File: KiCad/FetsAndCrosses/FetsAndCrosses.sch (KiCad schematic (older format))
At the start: 30 parts, among them J1 9Vdc, U1 L7805

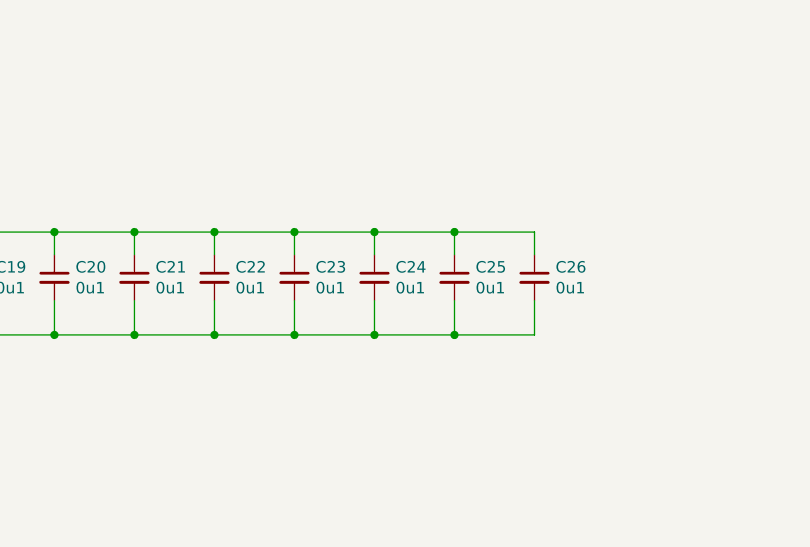
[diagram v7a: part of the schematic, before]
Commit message: Updated Schematic
 - Fixed Mem cell
 - Fixed Draw LED to not light if last move wins game
 - Changed capacitor
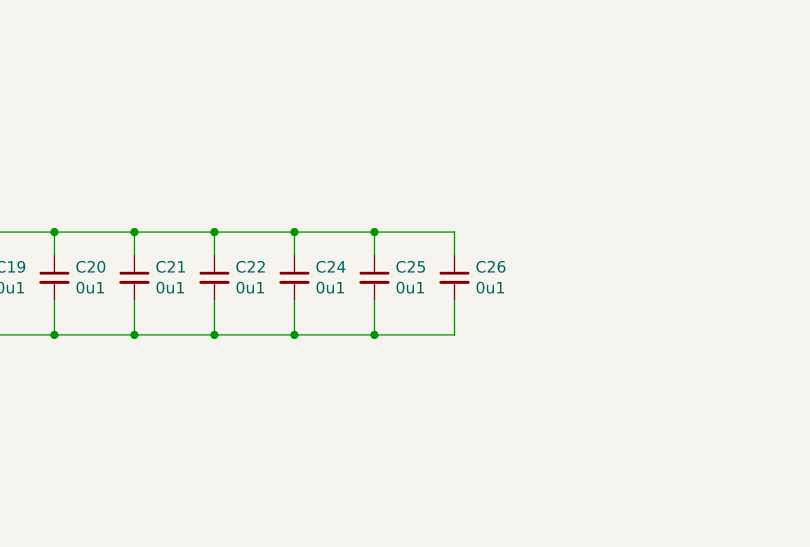
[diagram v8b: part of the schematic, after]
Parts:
- removed C23: 0u1, LogicQ:C_0603_1608Metric_NOLBL, symbol Device:C_Small
- C3: footprint Capacitor_Tantalum_SMD:CP_EIA-6032-15_Kemet-U -> Capacitor_SMD:CP_Elec_6.3x7.7
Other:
- moved on the sheet: C24, C25, C26
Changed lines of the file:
@@
 $Descr A3 16535 11693
 encoding utf-8
-Sheet 1 360
+Sheet 1 362
 Title "Fets and Crosses"
-Date "2020-08-28"
-Rev "v0.1"
+Date "2020-09-15"
+Rev "v0.2"
 Comp "Philipp Schilk"
 Comment1 "Tic-Tac-Toe implementation from discrete-transistor CMOS logic"
@@
 F 0 "C3" H 4141 9996 50  0000 L CNN
 F 1 "10u" H 4141 9905 50  0000 L CNN
-F 2 "Capacitor_Tantalum_SMD:CP_EIA-6032-15_Kemet-U" H 4050 9950 50  0001 C CNN
+F 2 "Capacitor_SMD:CP_Elec_6.3x7.7" H 4050 9950 50  0001 C CNN
 F 3 "~" H 4050 9950 50  0001 C CNN
 	1    4050 9950
@@
 $EndComp
 $Comp
-L Device:C_Small C23
-U 1 1 5F124EFA
+L Device:C_Small C24
+U 1 1 5F124F00
 P 9450 9950
-F 0 "C23" H 9542 9996 50  0000 L CNN
+F 0 "C24" H 9542 9996 50  0000 L CNN
 F 1 "0u1" H 9542 9905 50  0000 L CNN
 F 2 "LogicQ:C_0603_1608Metric_NOLBL" H 9450 9950 50  0001 C CNN
@@
 $EndComp
 $Comp
-L Device:C_Small C24
-U 1 1 5F124F00
+L Device:C_Small C25
+U 1 1 5F124F06
 P 9800 9950
-F 0 "C24" H 9892 9996 50  0000 L CNN
+F 0 "C25" H 9892 9996 50  0000 L CNN
 F 1 "0u1" H 9892 9905 50  0000 L CNN
 F 2 "LogicQ:C_0603_1608Metric_NOLBL" H 9800 9950 50  0001 C CNN
@@
 $EndComp
 $Comp
-L Device:C_Small C25
-U 1 1 5F124F06
+L Device:C_Small C26
+U 1 1 5F124F0C
 P 10150 9950
-F 0 "C25" H 10242 9996 50  0000 L CNN
+F 0 "C26" H 10242 9996 50  0000 L CNN
 F 1 "0u1" H 10242 9905 50  0000 L CNN
 F 2 "LogicQ:C_0603_1608Metric_NOLBL" H 10150 9950 50  0001 C CNN
@@
 	1    0    0    -1
 $EndComp
-$Comp
-L Device:C_Small C26
-U 1 1 5F124F0C
-P 10500 9950
-F 0 "C26" H 10592 9996 50  0000 L CNN
-F 1 "0u1" H 10592 9905 50  0000 L CNN
-F 2 "LogicQ:C_0603_1608Metric_NOLBL" H 10500 9950 50  0001 C CNN
-F 3 "~" H 10500 9950 50  0001 C CNN
-	1    10500 9950
-	1    0    0    -1
-$EndComp
-Wire Wire Line
-	10500 10200 10500 10050
-Wire Wire Line
-	10500 9750 10500 9850
-Wire Wire Line
-	10150 9850 10150 9750
-Connection ~ 10150 9750
-Wire Wire Line
-	10150 9750 10500 9750
+Wire Wire Line
+	10150 10200 10150 10050
+Wire Wire Line
+	10150 9750 10150 9850
 Wire Wire Line
 	9800 9850 9800 9750
@@
 Wire Wire Line
 	9450 9850 9450 9750
-Connection ~ 9450 9750
 Wire Wire Line
 	9450 9750 9800 9750
 Wire Wire Line
 	9100 9850 9100 9750
-Connection ~ 9100 9750
-Wire Wire Line
-	9100 9750 9450 9750
 Wire Wire Line
 	8750 9850 8750 9750
@@
 Wire Wire Line
 	9100 10050 9100 10200
-Connection ~ 9100 10200
 Wire Wire Line
 	9450 10050 9450 10200
-Wire Wire Line
-	9100 10200 9450 10200
-Connection ~ 9450 10200
 Wire Wire Line
 	9450 10200 9800 10200
@@
 Wire Wire Line
 	9800 10200 10150 10200
-Wire Wire Line
-	10150 10050 10150 10200
-Connection ~ 10150 10200
-Wire Wire Line
-	10150 10200 10500 10200
 Connection ~ 8400 9750
 Wire Wire Line
@@
 Wire Wire Line
 	4700 10200 4900 10200
+Wire Wire Line
+	9100 9750 9450 9750
+Connection ~ 9100 9750
+Connection ~ 9450 9750
+Wire Wire Line
+	9450 10200 9100 10200
+Connection ~ 9450 10200
+Connection ~ 9100 10200
 $EndSCHEMATC
